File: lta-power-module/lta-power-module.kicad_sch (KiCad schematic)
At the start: 29 parts

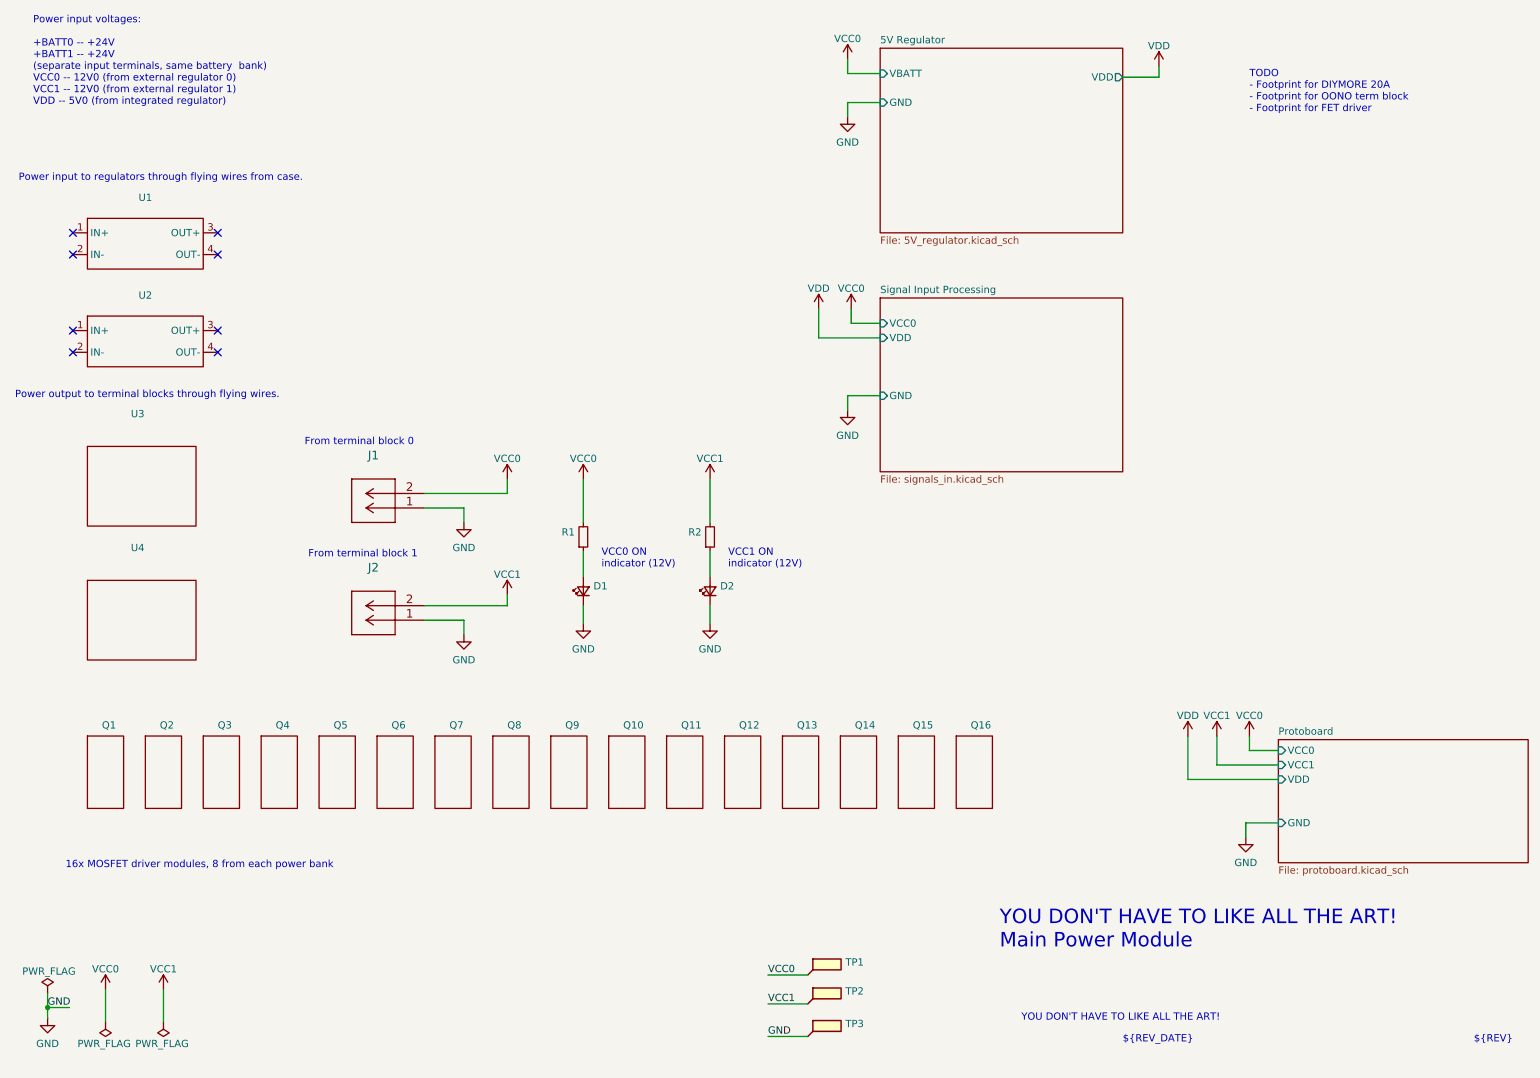
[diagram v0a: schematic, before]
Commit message: Considerably more work on power module PCB.
* Slight reorganization of layout.
* Routed all traces.
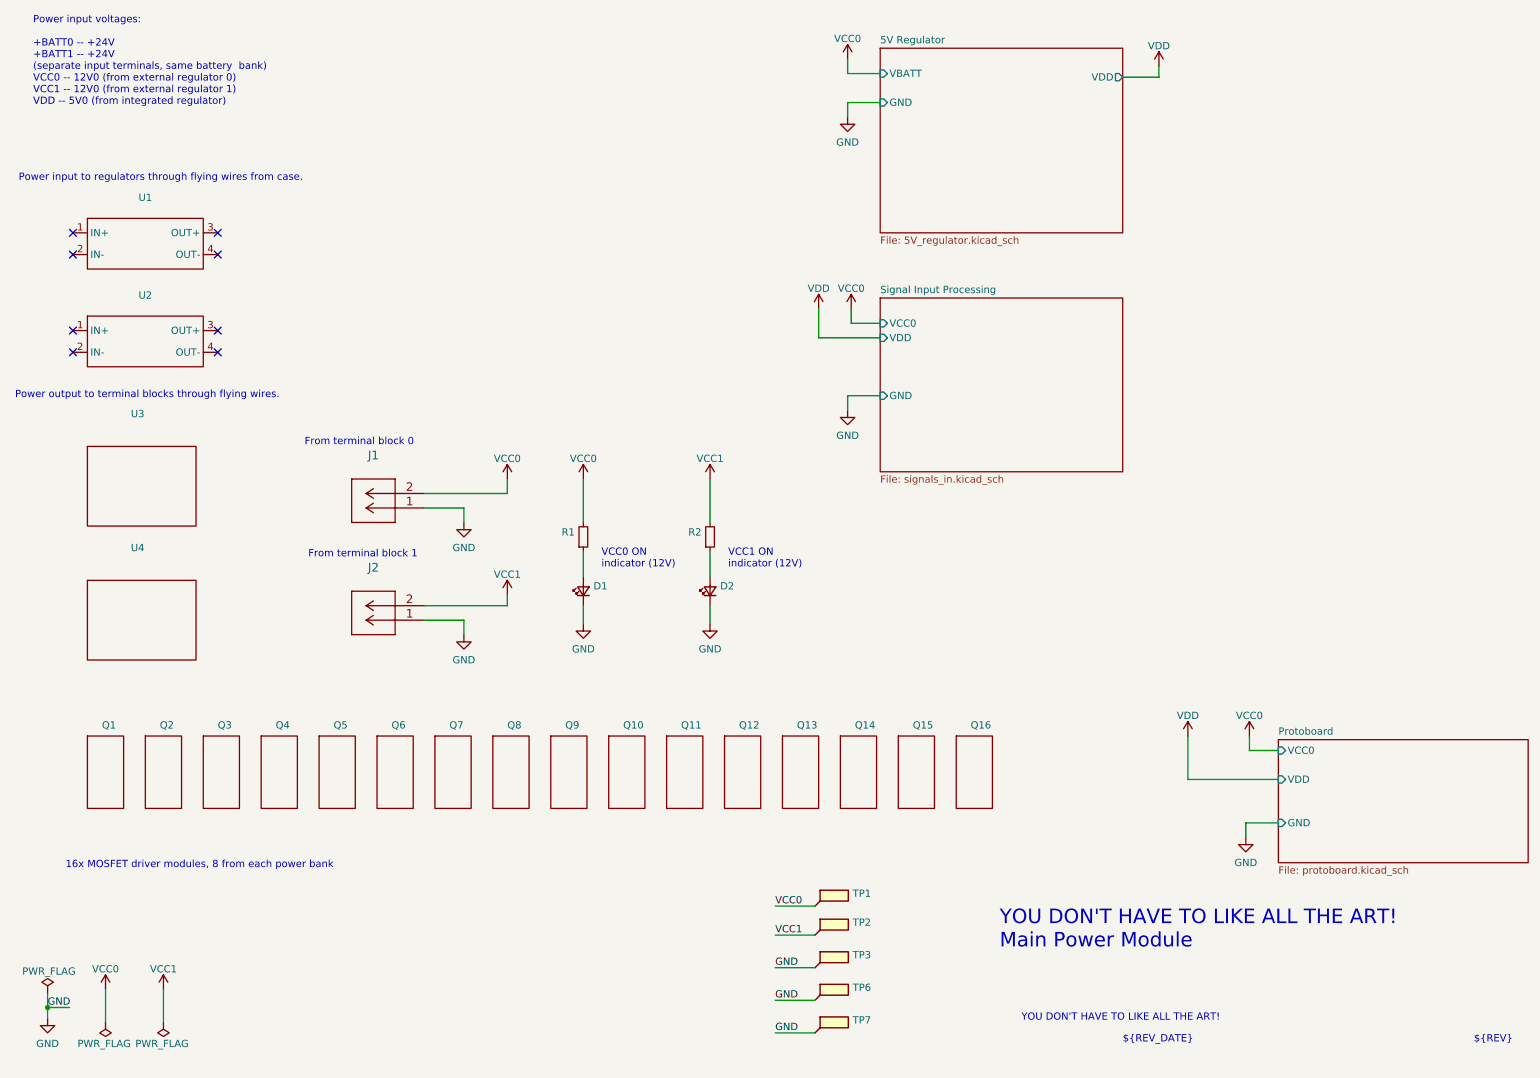
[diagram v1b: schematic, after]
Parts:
- added TP6, TP7: (no value), symbol Connector:TestPoint_Flag
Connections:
- net GND: now also TP6.1, TP7.1
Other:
- sheet Protoboard ports: added none; removed VCC1
- note removed: "TODO - Footprint for DIYMORE 20A - Footprint for OONO term block - Footprint for FET driver"
- moved on the sheet: TP1, TP2, TP3

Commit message: Add protoboard.
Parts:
- D1, D2: SPN (none) -> C5SMF-RJF-CT0W0BB1-ND; Supplier (none) -> DigiKey
- J1, J2: SPN (none) -> WM19004-ND; Supplier (none) -> DigiKey
- R1, R2: SPN (none) -> CF14JT1K00CT-ND; Supplier (none) -> DigiKey
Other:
- note added: "TODO: - Conform shape to polycase - Add several mounting holes (10x?) - Fix DIYMORE step down symbol - Double-check all big-block footprints"

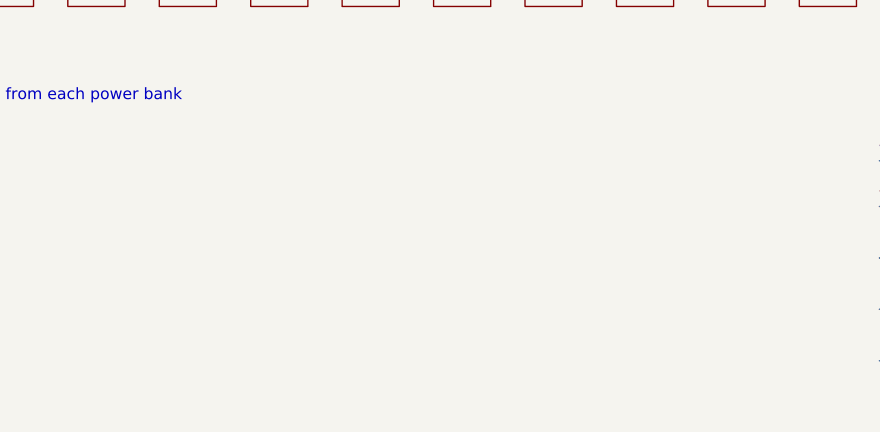
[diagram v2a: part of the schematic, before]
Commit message: Work on border.
* Add perimeter edge cut to fit WH-22 polycase.
* Add M5 mounting holes in temp locations on PCB.
* Lay out and lock left-edge M5 mounting holes.
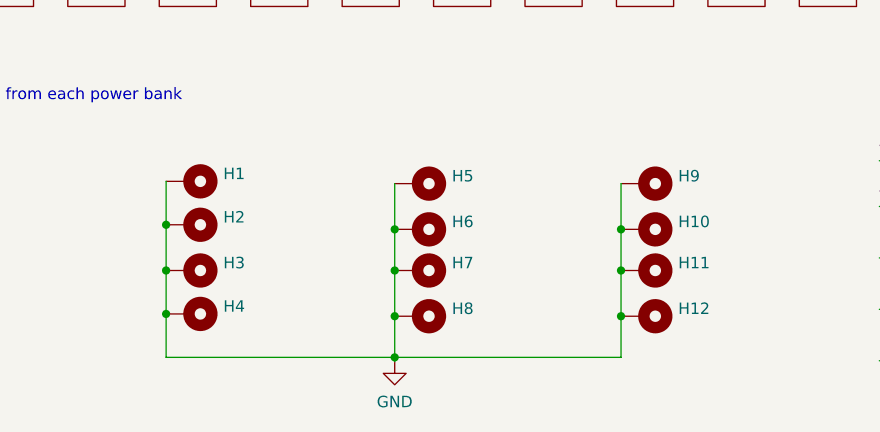
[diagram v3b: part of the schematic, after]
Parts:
- added H1, H10, H11, H12, H2, H3, H4, H5, H6, H7, H8, H9: (no value), symbol Mechanical:MountingHole_Pad
- J1, J2: Comment (none) -> 2-pin header for power (regulator out)
- Q1, Q10, Q11, Q12, Q13, Q14, Q15, Q16, Q2, Q3, Q4, Q5, Q6, Q7, Q8, Q9: Comment (none) -> Dual MOSFET driver board w/ mounting holes
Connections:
- net GND: now also H1.1, H10.1, H11.1, H12.1, H2.1, H3.1, H4.1, H5.1, H6.1, H7.1, H8.1, H9.1

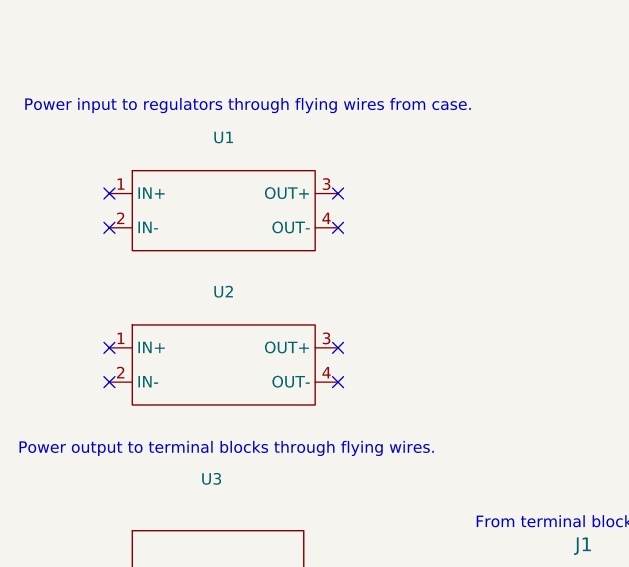
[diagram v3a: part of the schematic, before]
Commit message: Lay out all mounting holes.
* All DRC checks passing.
* Fix footprint silkscreen conflicts.
* Fix ext. regulator module symbol.
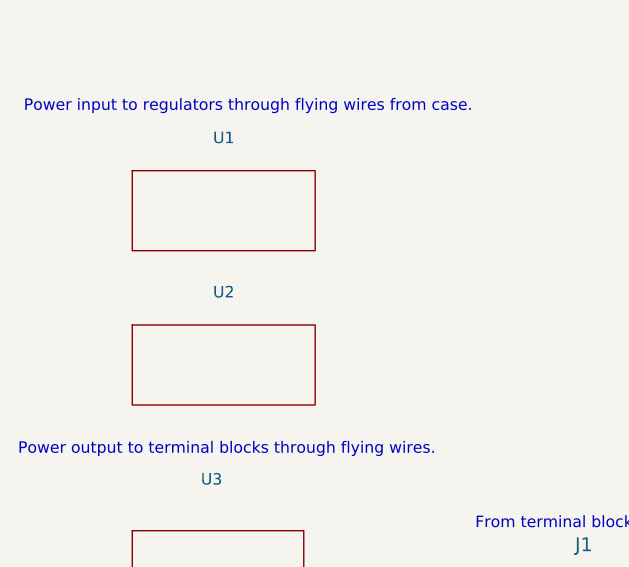
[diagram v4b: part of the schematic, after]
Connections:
- no-connect marks 8 -> 0
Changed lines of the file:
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@@
   (junction (at 92.202 192.024) (diameter 0) (color 0 0 0 0)
   )
-  (no_connect (at 22.86 73.025))
-  (no_connect (at 22.86 52.07))
-  (no_connect (at 48.26 52.07))
-  (no_connect (at 48.26 55.88))
-  (no_connect (at 22.86 55.88))
-  (no_connect (at 48.26 69.215))
-  (no_connect (at 22.86 69.215))
-  (no_connect (at 48.26 73.025))
   (wire (pts (xy 112.395 95.25) (xy 112.395 102.87))
     (stroke (width 0) (type default) (color 0 0 0 0))
@@
     )
   )
-  (symbol (lib_id "lta-power-syms:DIYMORE_20A_Step_Down") (at 22.86 69.215 0) (unit 1)
+  (symbol (lib_name "DIYMORE_20A_Step_Down_1") (lib_id "lta-power-syms:DIYMORE_20A_Step_Down") (at 22.86 69.215 0) (unit 1)
     (in_bom yes) (on_board yes) (fields_autoplaced)
     (property "Reference" "U2" (id 0) (at 35.56 63.026 0))
@@
       (effects (font (size 1.27 1.27)) hide)
     )
-    (pin "1")
-    (pin "2")
-    (pin "3")
-    (pin "4")
   )
   (symbol (lib_id "power:GND") (at 91.44 122.555 0) (unit 1)
@@
       (effects (font (size 1.27 1.27)) hide)
     )
-    (pin "1")
-    (pin "2")
-    (pin "3")
-    (pin "4")
   )
   (symbol (lib_id "lta-power-syms:VCC0") (at 159.385 65.405 0) (unit 1)
@@
     )
     (path "/918a6f77-0bf7-489a-8816-6cb55586b21f"
-      (reference "D1") (unit 1) (value "PWR0") (footprint "LED_THT:LED_D5.0mm")
+      (reference "D1") (unit 1) (value "PWR0") (footprint "Aaron_THT:LED_D5.0mm_SilkFix")
     )
     (path "/a463a5ce-b777-4109-bc29-6b5bd084145a"
-      (reference "D2") (unit 1) (value "PWR1") (footprint "LED_THT:LED_D5.0mm")
+      (reference "D2") (unit 1) (value "PWR1") (footprint "Aaron_THT:LED_D5.0mm_SilkFix")
     )
     (path "/19fe7b1f-5a54-4c9d-b474-e7909459658b/e4dee6ff-fb14-46ed-9a7d-3293759905ba"
@@
     )
     (path "/19fe7b1f-5a54-4c9d-b474-e7909459658b/a7b3af90-4139-44d8-9764-842a8952aeff"
-      (reference "D4") (unit 1) (value "5V0PWR") (footprint "LED_THT:LED_D5.0mm")
+      (reference "D4") (unit 1) (value "5V0PWR") (footprint "Aaron_THT:LED_D5.0mm_SilkFix")
     )
     (path "/69dcebde-2a18-481e-b4e9-936bbf72253b"

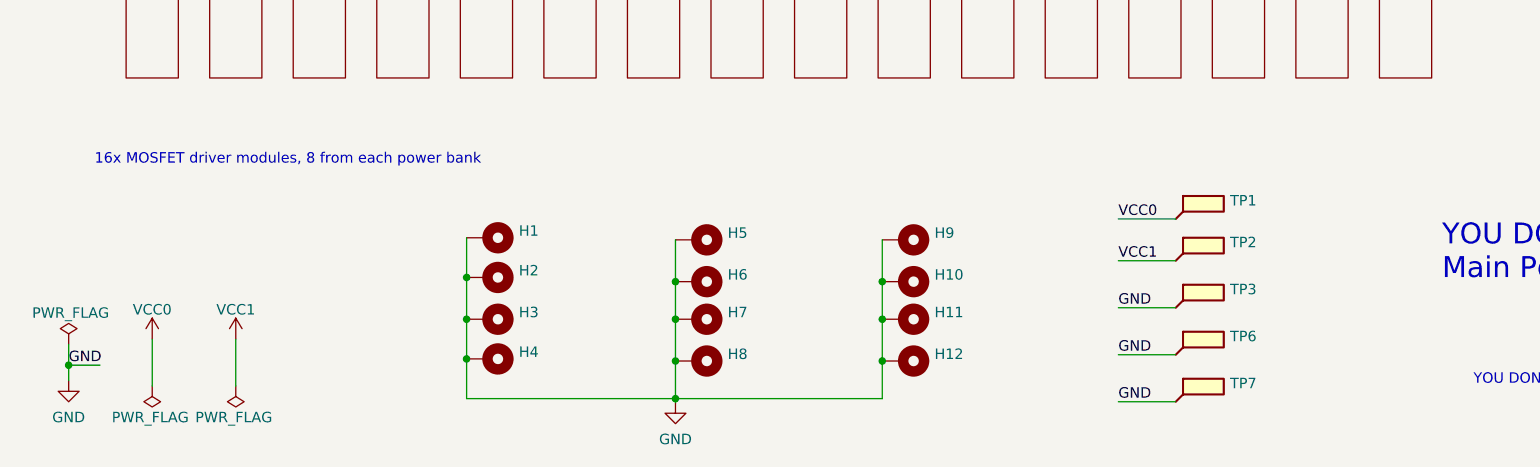
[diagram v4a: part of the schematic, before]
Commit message: NPTHs and test points.
* Added NPTH defs to `User.Eco1` layer in footprints.
* Renamed `User.Eco1` to `Mechanical` in PCB layout.
* Duplicated `Edge Cuts` onto `Mechanical` layer.
  *Use `Mechanical` as `.GKO` layer, not `Edge Cuts`!*
* Added test points for key signals.
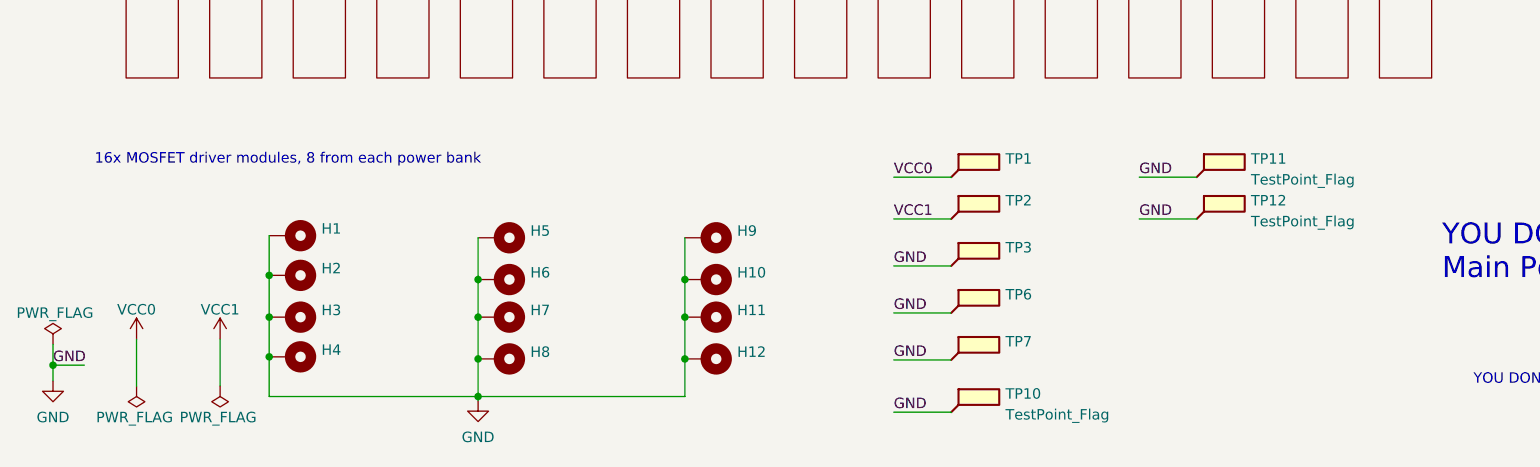
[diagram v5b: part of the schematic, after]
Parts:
- added TP10, TP11, TP12: TestPoint_Flag, Aaron_THT:TestPoint_THTPad_1.0x1.0mm_Drill0.3mm, symbol Connector:TestPoint_Flag
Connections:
- net GND: now also TP10.1, TP11.1, TP12.1
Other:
- moved on the sheet: H1, H10, H11, H12, H2, H3, H4, H5, H6, H7, H8, H9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
